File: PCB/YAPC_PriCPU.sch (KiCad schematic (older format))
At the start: 10 parts

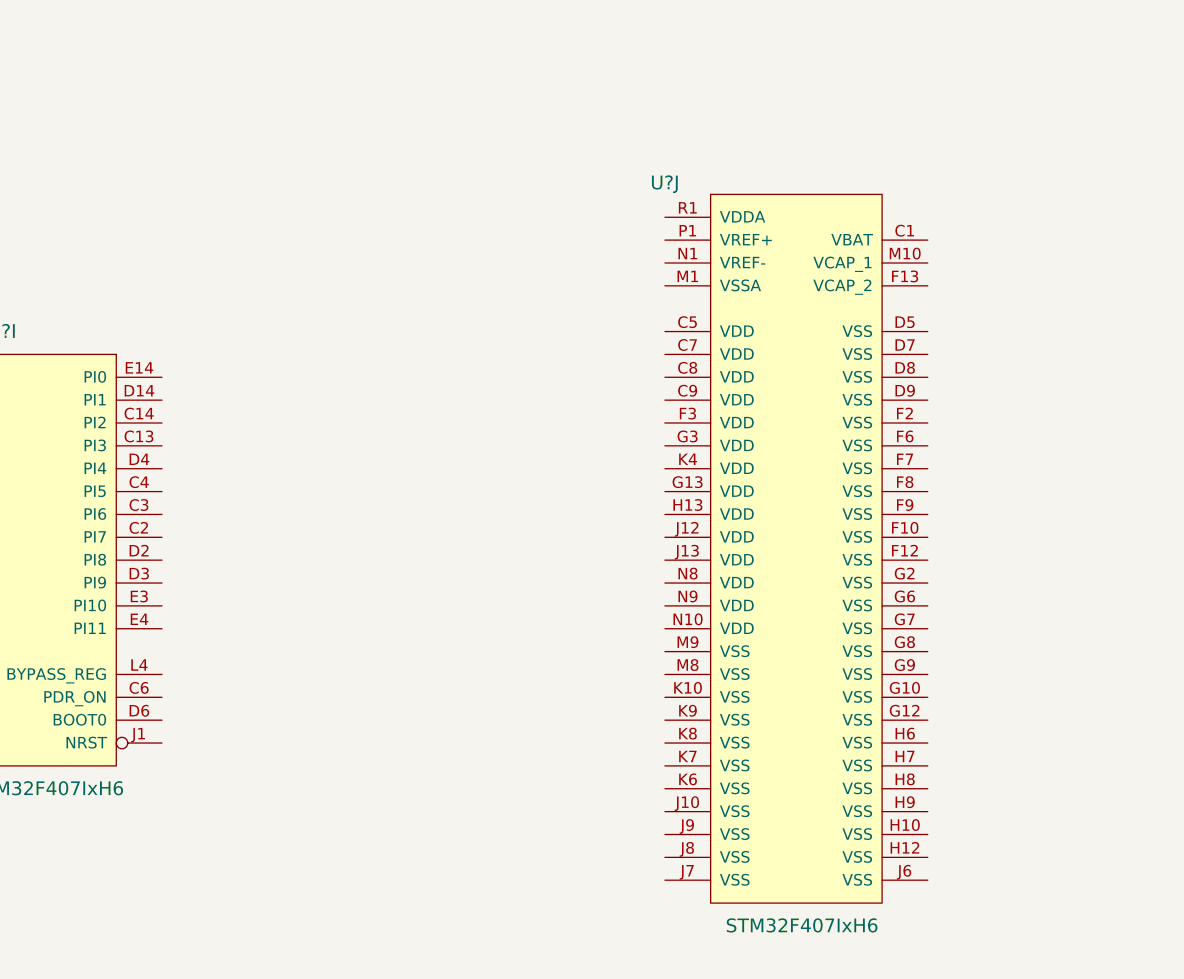
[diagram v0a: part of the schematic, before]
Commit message: Start applying power and config to the CPU
Start with the cpu power scheme and some of the external configuration
needed.
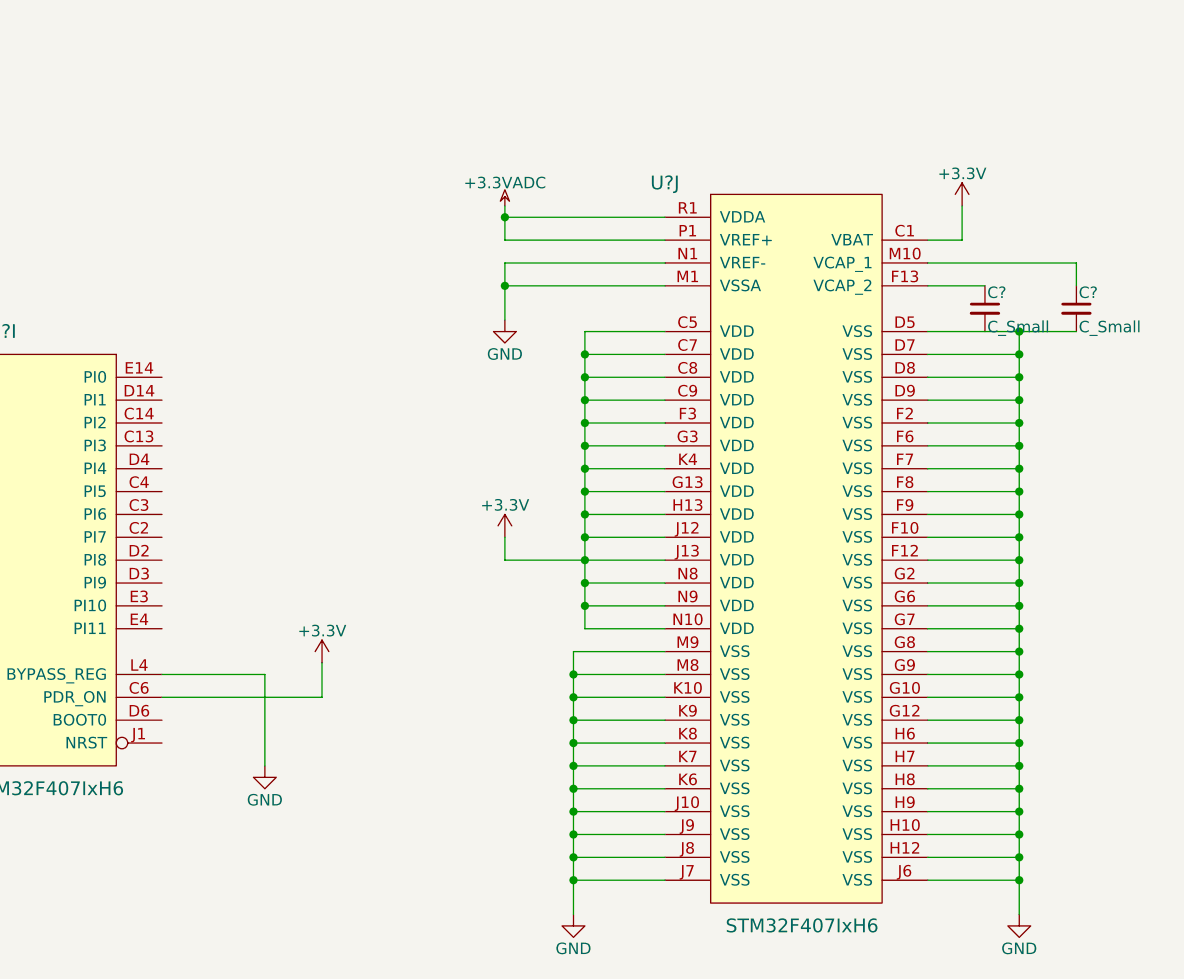
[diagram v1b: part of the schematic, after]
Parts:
- added C? (x2): C_Small, symbol C_Small
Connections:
- net +3V3: now reaches U?.C6 (PDR_ON)
- net +3V3: now also U?.C1 (VBAT), U?.C5 (VDD), U?.C7 (VDD), U?.C8 (VDD), U?.C9 (VDD), U?.F3 (VDD), U?.G13 (VDD), U?.G3 (VDD), U?.H13 (VDD), U?.J12 (VDD), U?.J13 (VDD), U?.K4 (VDD), U?.N10 (VDD), U?.N8 (VDD), U?.N9 (VDD)
- net GND: now reaches U?.L4 (BYPASS_REG)
- net GND: now also U?.D5 (VSS), U?.D7 (VSS), U?.D8 (VSS), U?.D9 (VSS), U?.F10 (VSS), U?.F12 (VSS), U?.F2 (VSS), U?.F6 (VSS), U?.F7 (VSS), U?.F8 (VSS), U?.F9 (VSS), U?.G10 (VSS), U?.G12 (VSS), U?.G2 (VSS), U?.G6 (VSS), U?.G7 (VSS), U?.G8 (VSS), U?.G9 (VSS), U?.H10 (VSS), U?.H12 (VSS), U?.H6 (VSS), U?.H7 (VSS), U?.H8 (VSS), U?.H9 (VSS), U?.J10 (VSS), U?.J6 (VSS), U?.J7 (VSS), U?.J8 (VSS), U?.J9 (VSS), U?.K10 (VSS), U?.K6 (VSS), U?.K7 (VSS), U?.K8 (VSS), U?.K9 (VSS), U?.M1 (VSSA), U?.M8 (VSS), U?.M9 (VSS), U?.N1 (VREF-), C?.2
- net at U?.F13 (VCAP_2): now also C?.1
- net at U?.M10 (VCAP_1): now also C?.1
- net +3.3VADC: now reaches U?.P1 (VREF+)
- net +3.3VADC: now also U?.R1 (VDDA)

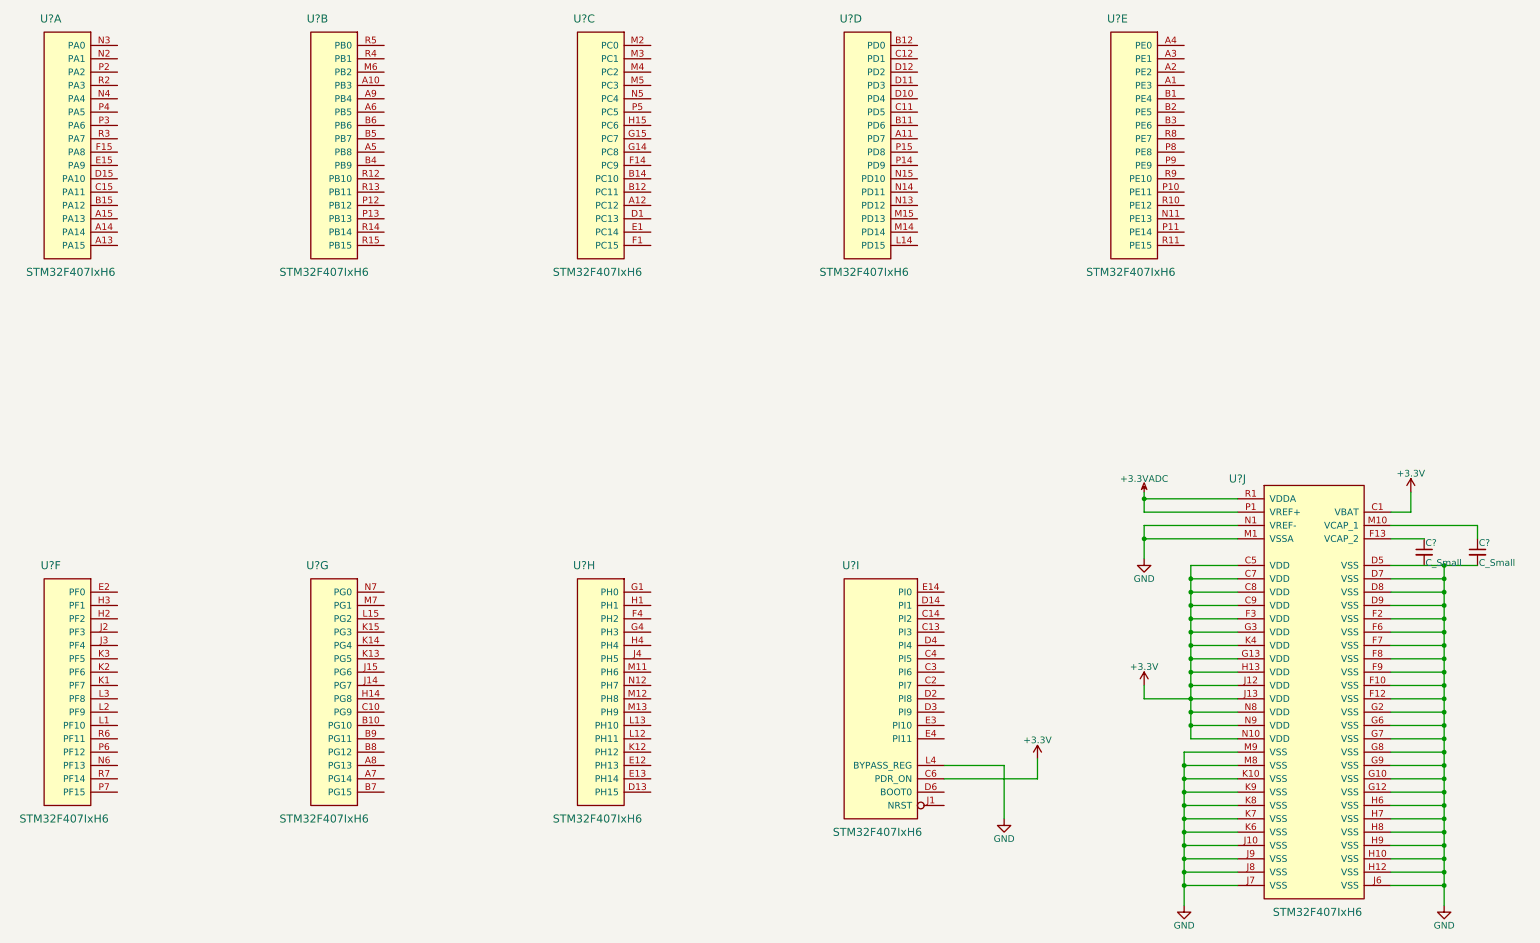
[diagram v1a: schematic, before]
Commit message: Start adding pin definitions
Allocate static function pins which cannot be moved
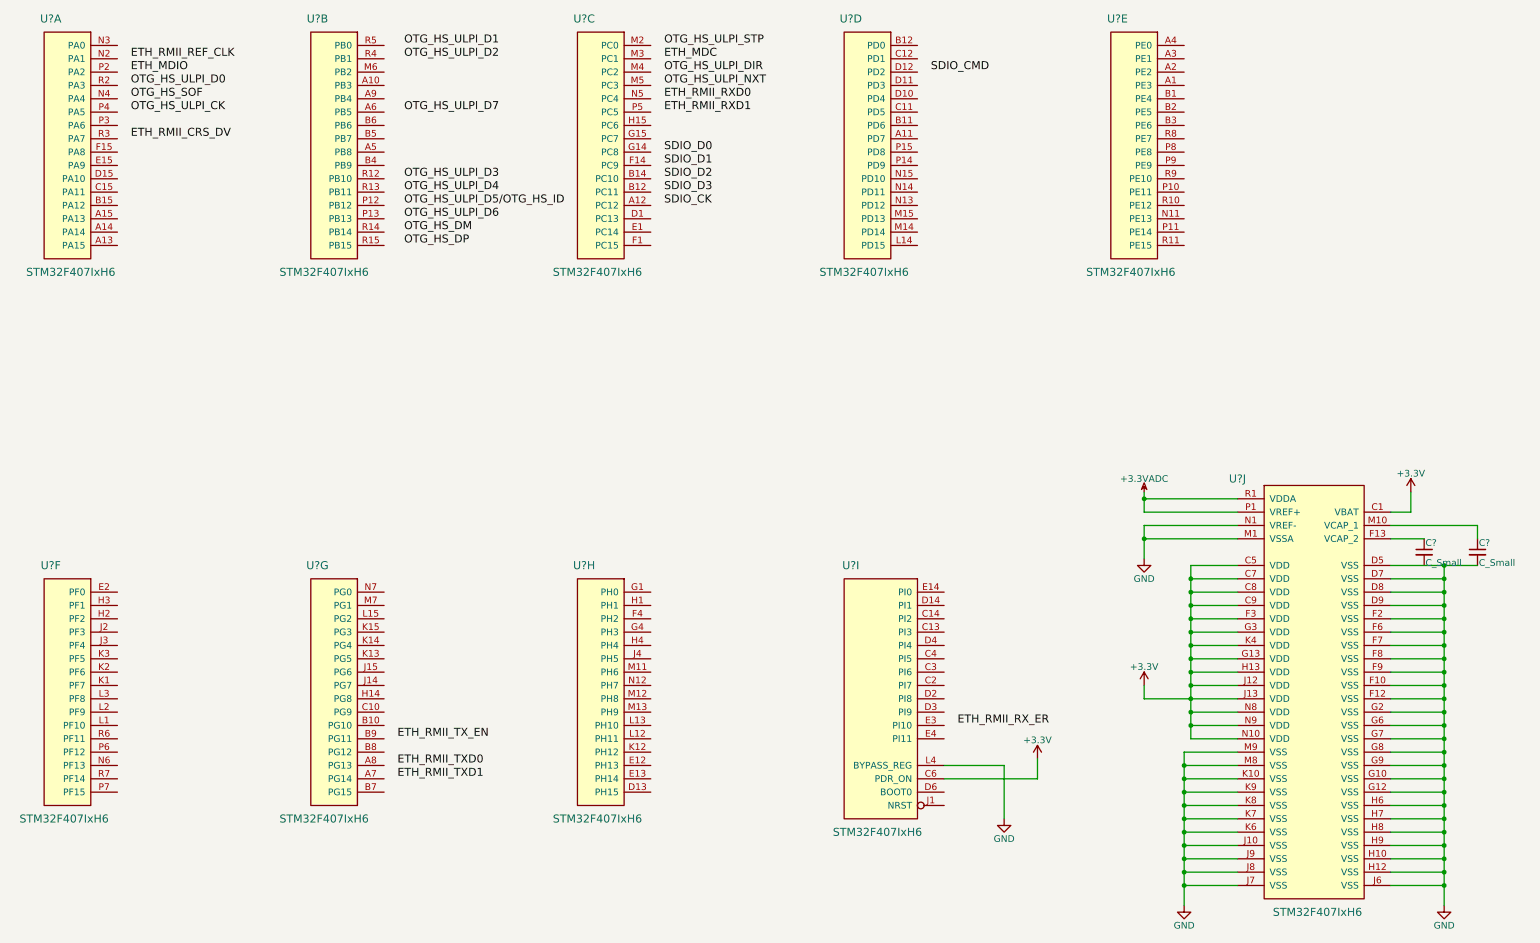
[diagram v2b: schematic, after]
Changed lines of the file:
@@
 Wire Wire Line
 	10150 7500 10150 7350
+Text Label 3350 2100 0    60   ~ 0
+ETH_RMII_REF_CLK
+Text Label 3350 2700 0    60   ~ 0
+ETH_RMII_CRS_DV
+Text Label 3350 2200 0    60   ~ 0
+ETH_MDIO
+Text Label 9550 7100 0    60   ~ 0
+ETH_RMII_RX_ER
+Text Label 5350 7200 0    60   ~ 0
+ETH_RMII_TX_EN
+Text Label 5350 7400 0    60   ~ 0
+ETH_RMII_TXD0
+Text Label 5350 7500 0    60   ~ 0
+ETH_RMII_TXD1
+Text Label 7350 2100 0    60   ~ 0
+ETH_MDC
+Text Label 7350 2400 0    60   ~ 0
+ETH_RMII_RXD0
+Text Label 7350 2500 0    60   ~ 0
+ETH_RMII_RXD1
+Text Label 3350 2300 0    60   ~ 0
+OTG_HS_ULPI_D0
+Text Label 3350 2500 0    60   ~ 0
+OTG_HS_ULPI_CK
+Text Label 5400 2000 0    60   ~ 0
+OTG_HS_ULPI_D1
+Text Label 5400 2100 0    60   ~ 0
+OTG_HS_ULPI_D2
+Text Label 5400 2500 0    60   ~ 0
+OTG_HS_ULPI_D7
+Text Label 5400 3000 0    60   ~ 0
+OTG_HS_ULPI_D3
+Text Label 5400 3100 0    60   ~ 0
+OTG_HS_ULPI_D4
+Text Label 5400 3200 0    60   ~ 0
+OTG_HS_ULPI_D5/OTG_HS_ID
+Text Label 5400 3300 0    60   ~ 0
+OTG_HS_ULPI_D6
+Text Label 7350 2000 0    60   ~ 0
+OTG_HS_ULPI_STP
+Text Label 7350 2200 0    60   ~ 0
+OTG_HS_ULPI_DIR
+Text Label 7350 2300 0    60   ~ 0
+OTG_HS_ULPI_NXT
+Text Label 5400 3400 0    60   ~ 0
+OTG_HS_DM
+Text Label 5400 3500 0    60   ~ 0
+OTG_HS_DP
+Text Label 3350 2400 0    60   ~ 0
+OTG_HS_SOF
+Text Label 7350 2800 0    60   ~ 0
+SDIO_D0
+Text Label 7350 2900 0    60   ~ 0
+SDIO_D1
+Text Label 7350 3000 0    60   ~ 0
+SDIO_D2
+Text Label 7350 3100 0    60   ~ 0
+SDIO_D3
+Text Label 7350 3200 0    60   ~ 0
+SDIO_CK
+Text Label 9350 2200 0    60   ~ 0
+SDIO_CMD
 $EndSCHEMATC

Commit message: Remove OTG_HS pins and use OTG_FS
So end users can recover boards with no additional hardware, the OTG_FS
port needs to be used for the integrated DFU
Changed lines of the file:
@@
 LIBS:valves
 LIBS:stm32f407ixh
+LIBS:lan8720a
 LIBS:YAPC-cache
 EELAYER 25 0
@@
 $Descr A3 16535 11693
 encoding utf-8
-Sheet 2 2
+Sheet 2 3
 Title ""
 Date ""
@@
 Text Label 7350 2500 0    60   ~ 0
 ETH_RMII_RXD1
-Text Label 3350 2300 0    60   ~ 0
-OTG_HS_ULPI_D0
-Text Label 3350 2500 0    60   ~ 0
-OTG_HS_ULPI_CK
-Text Label 5400 2000 0    60   ~ 0
-OTG_HS_ULPI_D1
-Text Label 5400 2100 0    60   ~ 0
-OTG_HS_ULPI_D2
-Text Label 5400 2500 0    60   ~ 0
-OTG_HS_ULPI_D7
-Text Label 5400 3000 0    60   ~ 0
-OTG_HS_ULPI_D3
-Text Label 5400 3100 0    60   ~ 0
-OTG_HS_ULPI_D4
-Text Label 5400 3200 0    60   ~ 0
-OTG_HS_ULPI_D5/OTG_HS_ID
-Text Label 5400 3300 0    60   ~ 0
-OTG_HS_ULPI_D6
-Text Label 7350 2000 0    60   ~ 0
-OTG_HS_ULPI_STP
-Text Label 7350 2200 0    60   ~ 0
-OTG_HS_ULPI_DIR
-Text Label 7350 2300 0    60   ~ 0
-OTG_HS_ULPI_NXT
-Text Label 5400 3400 0    60   ~ 0
-OTG_HS_DM
-Text Label 5400 3500 0    60   ~ 0
-OTG_HS_DP
-Text Label 3350 2400 0    60   ~ 0
-OTG_HS_SOF
 Text Label 7350 2800 0    60   ~ 0
 SDIO_D0
@@
 Text Label 9350 2200 0    60   ~ 0
 SDIO_CMD
+Text Label 3350 2900 0    60   ~ 0
+OTG_FS_VBUS
+Text Label 3350 3000 0    60   ~ 0
+OTG_FS_ID
+Text Label 3350 3100 0    60   ~ 0
+OTG_FS_DM
+Text Label 3350 3200 0    60   ~ 0
+OTG_FS_DP
 $EndSCHEMATC
